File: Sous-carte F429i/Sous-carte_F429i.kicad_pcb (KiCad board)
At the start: 2 copper layers, 157 parts, among them P1 CONN_01X02, P10 CONN_01X01, P100 CONN_01X01, P101 CONN_01X01, P102 CONN_01X01, P103 CONN_01X01, P104 CONN_01X01, P105 CONN_01X01, P106 CONN_01X01, P107 CONN_01X01, P108 CONN_01X01, P109 CONN_01X01, P11 CONN_01X02, P110 CONN_01X01, P111 CONN_01X01, P112 CONN_01X01, P113 CONN_01X01, P114 CONN_01X01, P115 CONN_01X01, P116 CONN_01X01, P117 CONN_01X01, P12 CONN_01X02, P13 CONN_01X03, P14 CONN_01X03, P15 CONN_01X02, P16 CONN_01X02, P17 CONN_01X02, P18 CONN_01X01, P19 CONN_01X01, P2 CONN_01X02, P20 CONN_01X01, P21 CONN_01X01, P22 CONN_01X01, P23 CONN_01X01, P24 CONN_01X01, P25 CONN_01X01, P26 CONN_01X01, P27 CONN_01X01, P28 CONN_01X01, P29 CONN_01X01, P3 CONN_01X02, P30 CONN_01X01, P31 CONN_01X01, P32 CONN_01X01, P33 CONN_01X01, P34 CONN_01X01, P35 CONN_01X01, P36 CONN_01X01, P37 CONN_01X01, P38 CONN_01X01, P39 CONN_01X01, P4 CONN_01X02, P40 CONN_01X01, P41 CONN_01X01, P42 CONN_01X01, P43 CONN_01X01, P44 CONN_01X01, P45 CONN_01X01, P46 CONN_01X01, P47 CONN_01X01, P48 CONN_01X01, P49 CONN_01X01, P5 CONN_01X02, P50 CONN_01X01, P51 CONN_01X01, P52 CONN_01X01, P53 CONN_01X01, P54 CONN_01X01, P55 CONN_01X01, P56 CONN_01X01, P57 CONN_01X01, P58 CONN_01X01, P59 CONN_01X01, P6 CONN_01X02, P60 CONN_01X01, P61 CONN_01X01, P62 CONN_01X01, P63 CONN_01X01, P64 CONN_01X01, P65 CONN_01X01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

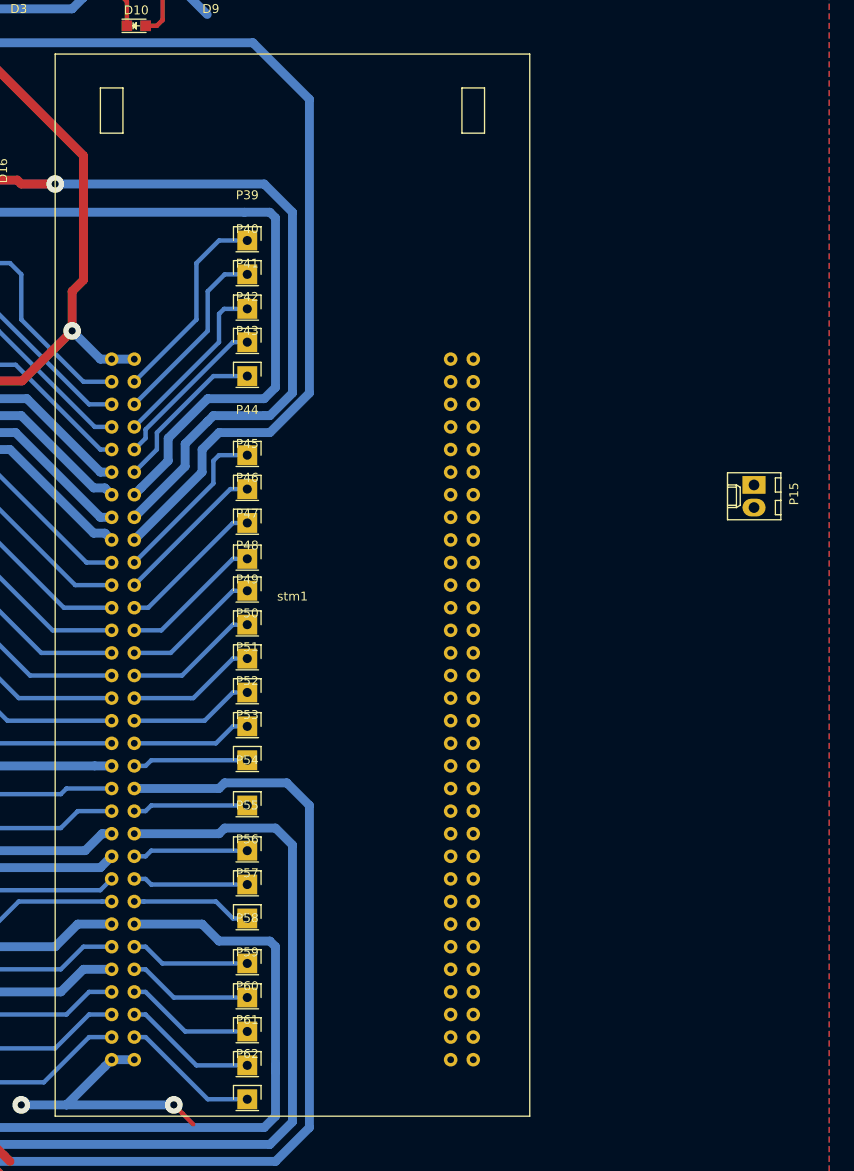
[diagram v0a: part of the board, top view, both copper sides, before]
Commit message: fix empreinte stm32
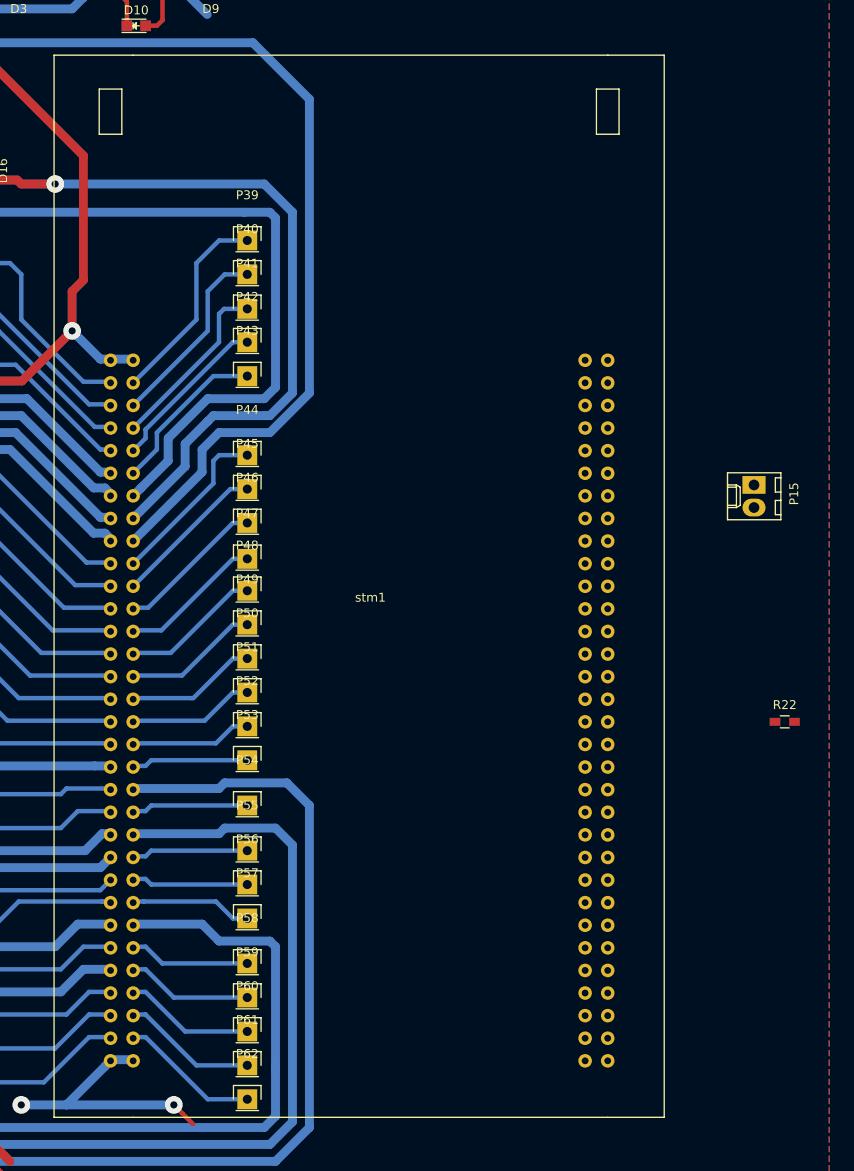
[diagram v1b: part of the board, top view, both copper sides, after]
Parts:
- added R22: R, Resistors_SMD:R_0603_HandSoldering, F.Cu at (243.9, 118.9)
- P29: value CONN_01X01 -> CONN_01X02
- moved stm1 8.76 mm to (197.4, 103.6)
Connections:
- P29 pad 1: Net-(P29-Pad1) -> +5V
- stm1 pad 33: Net-(P29-Pad1) -> EQUIPE
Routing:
- net (no net): track 0.00 -> 138.7 mm, vias 0 -> 4
- net USART2_TX: track 184.5 -> 115.9 mm, vias 1 -> 0
- net SWITCH_0: track 166.5 -> 126.4 mm, vias 2 -> 1
- net GND: track 513.1 -> 483.2 mm, vias 8 -> 6
- net Net-(P29-Pad1): track 15.1 -> 0.00 mm
- net +5V: track 225.8 -> 240.9 mm

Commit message: changement footprint stm32 sur le pcb
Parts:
- removed P29: CONN_01X02, Pin_Headers:Pin_Header_Straight_1x01
- moved P10 110.0 mm to (253.9, 139.5)
- moved P14 110.0 mm to (250.1, 151.0)
- moved R10 110.0 mm to (248.6, 129.6)
- moved R12 110.0 mm to (248.6, 109.3)
- moved R9 110.0 mm to (248.6, 125.8)
- moved D11 110.0 mm to (257.7, 145.0)
- moved D12 110.0 mm to (247.7, 87.3)
- moved D13 110.0 mm to (247.7, 100.0)
- moved P100 110.0 mm to (238.6, 98.5)
- moved P102 110.0 mm to (238.6, 108.0)
- moved P103 110.0 mm to (238.6, 111.9)
- moved P104 110.0 mm to (238.6, 115.7)
- moved P105 110.0 mm to (238.6, 119.5)
- moved P106 110.0 mm to (238.6, 123.3)
- moved P107 110.0 mm to (238.6, 127.1)
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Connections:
- stm1 pad 68: Net-(stm1-Pad68) -> (no net)
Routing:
- net (no net): track 138.7 -> 0.00 mm, vias 4 -> 0
- net USART2_TX: track 115.9 -> 203.5 mm, vias 0 -> 1
- net GND: track 483.2 -> 563.7 mm, vias 6 -> 8
- net SWITCH_0: track 126.4 -> 182.4 mm, vias 1 -> 2
- net EQUIPE: track 0.00 -> 20.5 mm, vias 0 -> 1
- net +BATT: track 177.4 -> 194.1 mm
- net +5V: track 240.9 -> 246.1 mm

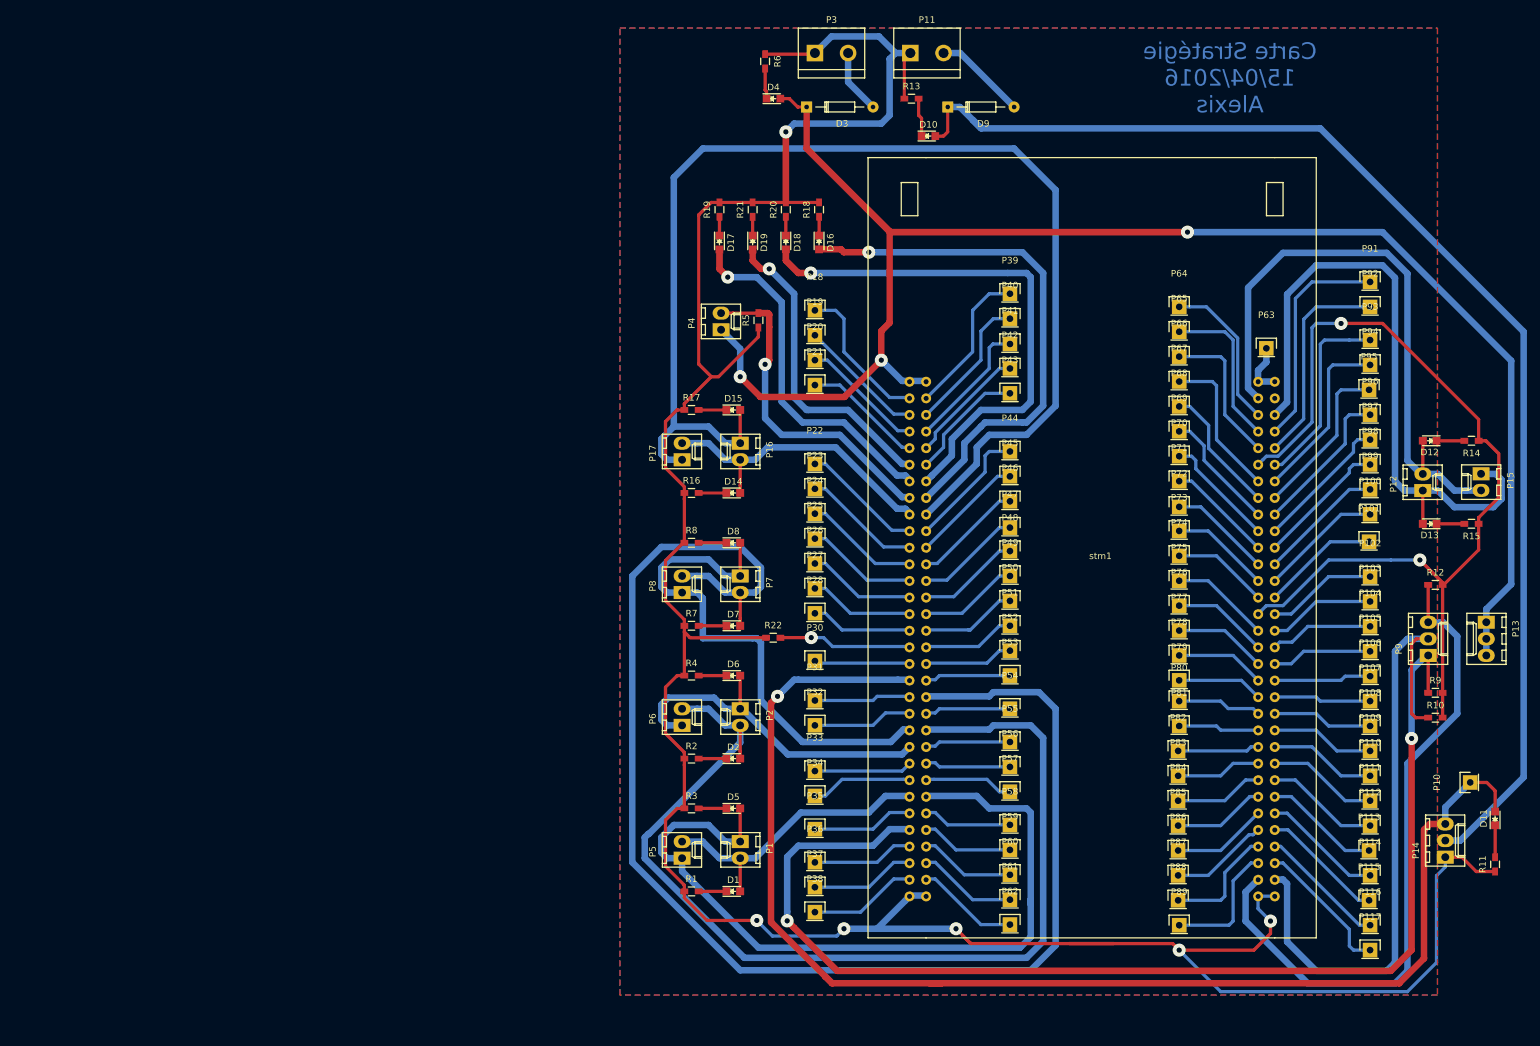
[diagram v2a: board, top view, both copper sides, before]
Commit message: Redimensionnement carte
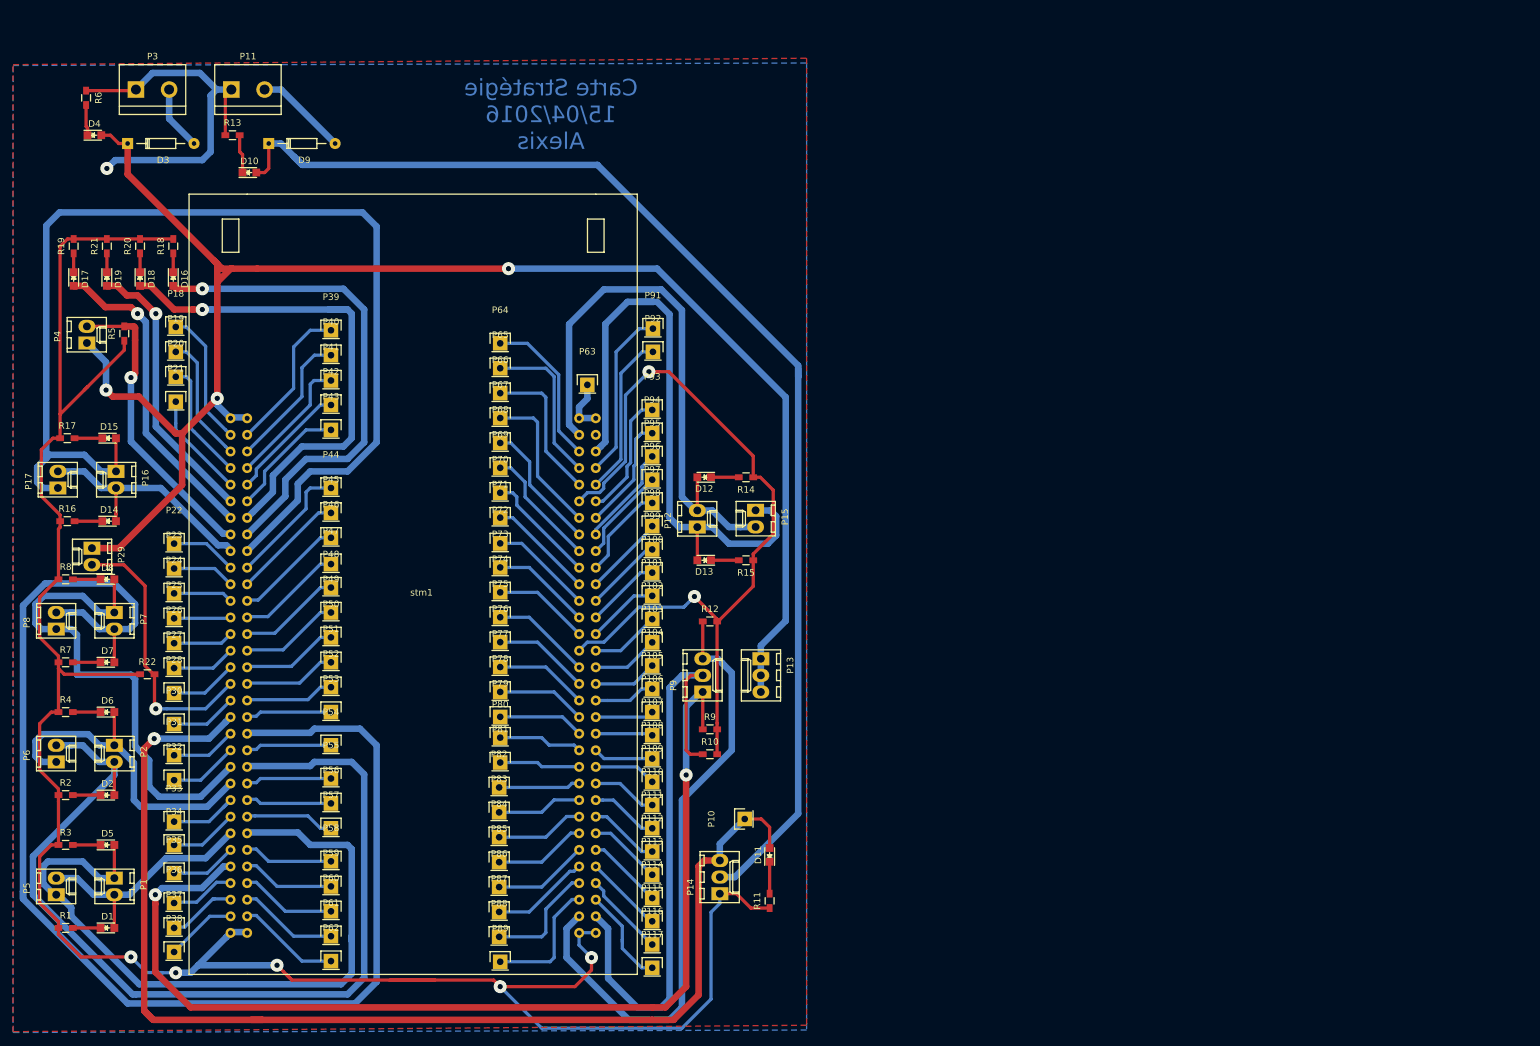
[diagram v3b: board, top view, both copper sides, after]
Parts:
- added P29: CONN_01X02, Connectors_Molex:Molex_KK_6410-02, F.Cu at (43.1, 103.7)
- moved D11 111.1 mm to (146.7, 150.6)
- moved P12 111.1 mm to (135.7, 100.5)
- moved R11 111.1 mm to (146.7, 157.7)
- moved D12 111.1 mm to (136.7, 92.8)
- moved D13 111.1 mm to (136.7, 105.5)
- moved P10 111.1 mm to (142.9, 145.1)
- moved P13 111.1 mm to (145.4, 120.6)
- moved P14 111.1 mm to (139.1, 156.6)
- moved P15 111.1 mm to (144.6, 97.9)
- moved P9 111.1 mm to (136.5, 125.7)
- moved R10 111.1 mm to (137.6, 135.2)
- moved R12 111.1 mm to (137.6, 114.9)
- moved R14 111.1 mm to (143.1, 92.8)
- moved R15 111.1 mm to (143.1, 105.5)
- moved R9 111.1 mm to (137.6, 131.4)
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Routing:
- net GND: track 563.7 -> 523.2 mm
- net EQUIPE: track 20.5 -> 42.1 mm
- net SWITCH_0: track 182.4 -> 161.9 mm
- net USART2_TX: track 203.5 -> 184.8 mm
- net UART8_TX: track 186.8 -> 173.7 mm
- net +5V: track 246.1 -> 259.2 mm
- net UART5_RX: track 218.5 -> 206.5 mm
- net UART4_RX: track 159.7 -> 148.5 mm
- net Net-(P93-Pad1): track 29.8 -> 19.1 mm
- net USART1_TX: track 122.4 -> 111.7 mm
- net Net-(P95-Pad1): track 25.0 -> 15.5 mm
- net UART8_RX: track 46.1 -> 36.6 mm
- net Net-(P94-Pad1): track 27.2 -> 18.2 mm
- net Net-(P24-Pad1): track 17.8 -> 9.11 mm
- net Net-(P23-Pad1): track 18.3 -> 9.64 mm
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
